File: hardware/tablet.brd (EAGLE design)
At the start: 198 x 124 mm, 0 parts

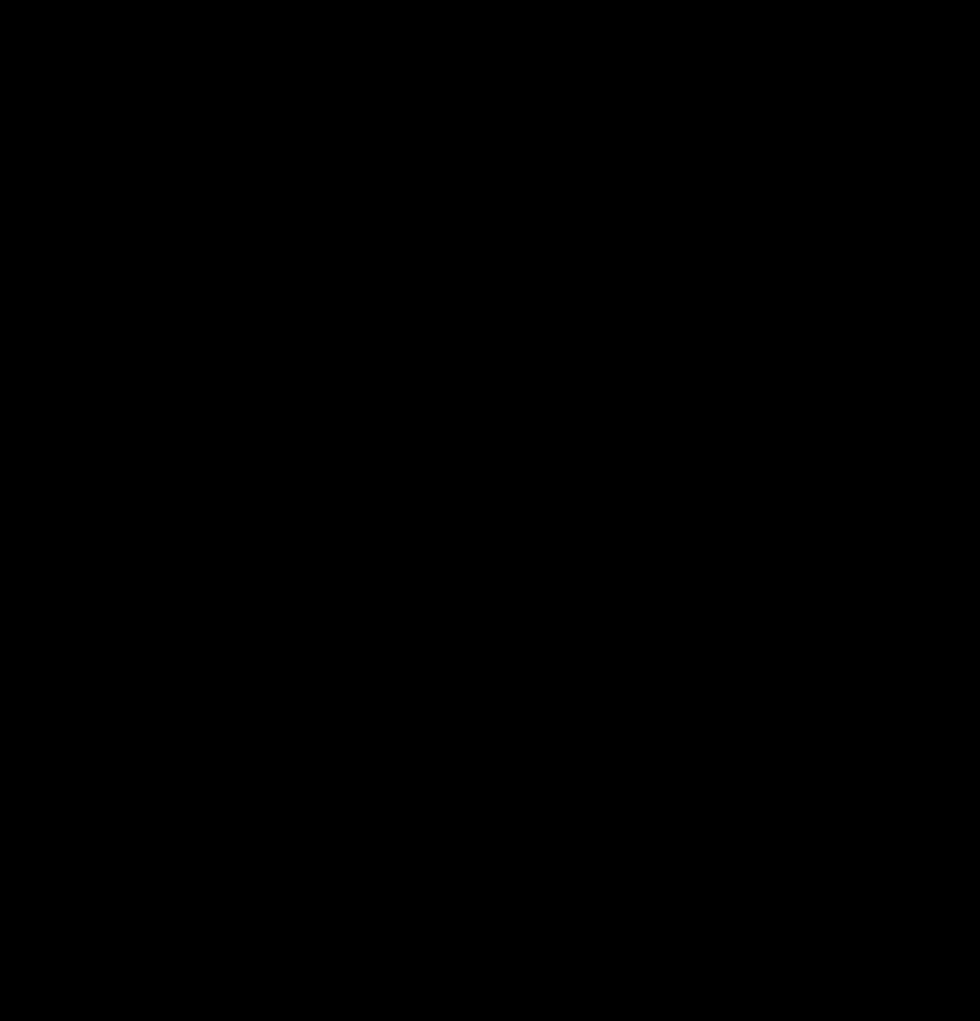
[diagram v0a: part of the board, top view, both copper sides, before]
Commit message: Initial analog front end schematic
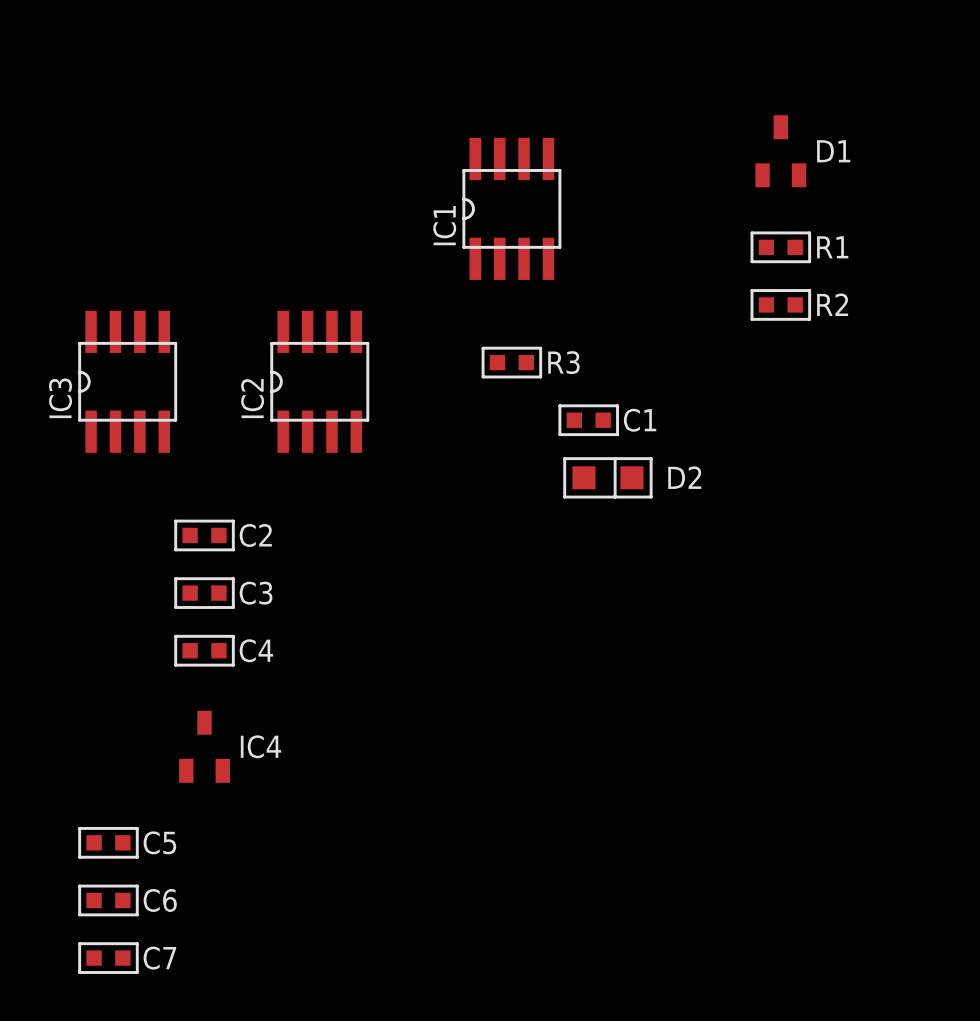
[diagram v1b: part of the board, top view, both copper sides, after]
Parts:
- added C1: ~470pF, 0jpe:0603
- added C2, C3, C4, C5, C6, C7: 100nF, 0jpe:0603
- added D1: BAT721S, 0jpe:SOT23_3
- added D2: 3V9, 0jpe:SOD323
- added IC1: (no value), 0jpe:SOIC8
- added IC2: MCP3201, 0jpe:SOIC8
- added IC3: DG9233EDY, 0jpe:SOIC8
- added IC4: MAX6104EUR, 0jpe:SOT23_3
- added R1: TBD, 0jpe:0603
- added R2, R3: 1K, 0jpe:0603
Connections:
- new net +5V: C2.1, C4.1, C5.1, C7.1, IC1.8, IC2.8, IC3.8, IC4.1
- new net -5V: C3.2, IC1.4
- new net ADC_CS: IC2.5
- new net GND: C2.2, C3.1, C4.2, C5.2, C6.2, C7.2, IC1.2, IC1.5, IC2.3, IC2.4, IC3.4, IC4.3
- new net INT_EN: IC3.7
- new net INT_RST: IC3.3
- new net MISO: IC2.6
- new net N$1: D1.1, IC3.2, R1.2
- new net N$2: D1.2, IC1.3, R1.1, R2.2
- new net N$3: D1.3, IC1.1
- new net N$4: C1.2, D2.1, IC1.6, IC3.6, R3.2
- new net N$6: C6.1, IC2.1, IC4.2
- new net N$7: IC3.1, R3.1
- new net SCLK: IC2.7
- new net SIG: R2.1
- new net VOUT: C1.1, D2.2, IC1.7, IC2.2, IC3.5
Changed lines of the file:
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@@
 </autorouter>
 <elements>
+<element name="D1" library="0jpe" package="SOT23_3" value="BAT721S" x="-99" y="-80"/>
+<element name="R1" library="0jpe" package="0603" value="TBD" x="-99" y="-85"/>
+<element name="R2" library="0jpe" package="0603" value="1K" x="-99" y="-88"/>
+<element name="IC1" library="0jpe" package="SOIC8" value="" x="-113" y="-83"/>
+<element name="R3" library="0jpe" package="0603" value="1K" x="-113" y="-91"/>
+<element name="C1" library="0jpe" package="0603" value="~470pF" x="-109" y="-94"/>
+<element name="D2" library="0jpe" package="SOD323" value="3V9" x="-108" y="-97"/>
+<element name="IC2" library="0jpe" package="SOIC8" value="MCP3201" x="-123" y="-92"/>
+<element name="IC3" library="0jpe" package="SOIC8" value="DG9233EDY" x="-133" y="-92"/>
+<element name="C2" library="0jpe" package="0603" value="100nF" x="-129" y="-100"/>
+<element name="C3" library="0jpe" package="0603" value="100nF" x="-129" y="-103"/>
+<element name="C4" library="0jpe" package="0603" value="100nF" x="-129" y="-106"/>
+<element name="IC4" library="0jpe" package="SOT23_3" value="MAX6104EUR" x="-129" y="-111"/>
+<element name="C5" library="0jpe" package="0603" value="100nF" x="-134" y="-116"/>
+<element name="C6" library="0jpe" package="0603" value="100nF" x="-134" y="-119"/>
+<element name="C7" library="0jpe" package="0603" value="100nF" x="-134" y="-122"/>
 </elements>
 <signals>
+<signal name="N$1">
+<contactref element="D1" pad="1"/>
+<contactref element="R1" pad="2"/>
+<contactref element="IC3" pad="2"/>
+<wire x1="-99.95" y1="-81.25" x2="-133.635" y2="-94.6" width="0" layer="19" extent="1-1"/>
+<wire x1="-98.25" y1="-85" x2="-99.95" y2="-81.25" width="0" layer="19" extent="1-1"/>
+</signal>
+<signal name="N$2">
+<contactref element="D1" pad="2"/>
+<contactref element="R2" pad="2"/>
+<contactref element="R1" pad="1"/>
+<contactref element="IC1" pad="3"/>
+<wire x1="-99.75" y1="-85" x2="-112.365" y2="-85.6" width="0" layer="19" extent="1-1"/>
+<wire x1="-98.25" y1="-88" x2="-99.75" y2="-85" width="0" layer="19" extent="1-1"/>
+<wire x1="-98.05" y1="-81.25" x2="-99.75" y2="-85" width="0" layer="19" extent="1-1"/>
+</signal>
+<signal name="N$3">
+<contactref element="D1" pad="3"/>
+<contactref element="IC1" pad="1"/>
+<wire x1="-99" y1="-78.75" x2="-114.905" y2="-85.6" width="0" layer="19" extent="1-1"/>
+</signal>
+<signal name="SIG">
+<contactref element="R2" pad="1"/>
+</signal>
+<signal name="GND">
+<contactref element="IC1" pad="2"/>
+<contactref element="IC1" pad="5"/>
+<contactref element="IC2" pad="3"/>
+<contactref element="IC2" pad="4"/>
+<contactref element="IC3" pad="4"/>
+<contactref element="C3" pad="1"/>
+<contactref element="C2" pad="2"/>
+<contactref element="C4" pad="2"/>
+<contactref element="IC4" pad="3"/>
+<contactref element="C5" pad="2"/>
+<contactref element="C6" pad="2"/>
+<contactref element="C7" pad="2"/>
+<wire x1="-133.25" y1="-116" x2="-133.25" y2="-119" width="0" layer="19" extent="1-1"/>
+<wire x1="-133.25" y1="-122" x2="-133.25" y2="-119" width="0" layer="19" extent="1-1"/>
+<wire x1="-129" y1="-109.75" x2="-133.25" y2="-116" width="0" layer="19" extent="1-1"/>
+<wire x1="-128.25" y1="-106" x2="-129" y2="-109.75" width="0" layer="19" extent="1-1"/>
+<wire x1="-129.75" y1="-103" x2="-128.25" y2="-106" width="0" layer="19" extent="1-1"/>
+<wire x1="-128.25" y1="-100" x2="-129.75" y2="-103" width="0" layer="19" extent="1-1"/>
+<wire x1="-131.095" y1="-94.6" x2="-128.25" y2="-100" width="0" layer="19" extent="1-1"/>
+<wire x1="-122.365" y1="-94.6" x2="-128.25" y2="-100" width="0" layer="19" extent="1-1"/>
+<wire x1="-121.095" y1="-94.6" x2="-122.365" y2="-94.6" width="0" layer="19" extent="1-1"/>
+<wire x1="-113.635" y1="-85.6" x2="-121.095" y2="-94.6" width="0" layer="19" extent="1-1"/>
+<wire x1="-111.095" y1="-80.4" x2="-113.635" y2="-85.6" width="0" layer="19" extent="1-1"/>
+</signal>
+<signal name="+5V">
+<contactref element="IC1" pad="8"/>
+<contactref element="IC3" pad="8"/>
+<contactref element="C2" pad="1"/>
+<contactref element="C4" pad="1"/>
+<contactref element="IC4" pad="1"/>
+<contactref element="C5" pad="1"/>
+<contactref element="IC2" pad="8"/>
+<contactref element="C7" pad="1"/>
+<wire x1="-134.75" y1="-122" x2="-134.75" y2="-116" width="0" layer="19" extent="1-1"/>
+<wire x1="-129.95" y1="-112.25" x2="-134.75" y2="-116" width="0" layer="19" extent="1-1"/>
+<wire x1="-129.75" y1="-106" x2="-129.95" y2="-112.25" width="0" layer="19" extent="1-1"/>
+<wire x1="-129.75" y1="-100" x2="-129.75" y2="-106" width="0" layer="19" extent="1-1"/>
+<wire x1="-124.905" y1="-89.4" x2="-129.75" y2="-100" width="0" layer="19" extent="1-1"/>
+<wire x1="-134.905" y1="-89.4" x2="-124.905" y2="-89.4" width="0" layer="19" extent="1-1"/>
+<wire x1="-114.905" y1="-80.4" x2="-124.905" y2="-89.4" width="0" layer="19" extent="1-1"/>
+</signal>
+<signal name="-5V">
+<contactref element="IC1" pad="4"/>
+<contactref element="C3" pad="2"/>
+<wire x1="-111.095" y1="-85.6" x2="-128.25" y2="-103" width="0" layer="19" extent="1-1"/>
+</signal>
+<signal name="N$4">
+<contactref element="IC1" pad="6"/>
+<contactref element="R3" pad="2"/>
+<contactref element="C1" pad="2"/>
+<contactref element="D2" pad="1"/>
+<contactref element="IC3" pad="6"/>
+<wire x1="-112.25" y1="-91" x2="-132.365" y2="-89.4" width="0" layer="19" extent="1-1"/>
+<wire x1="-108.25" y1="-94" x2="-112.25" y2="-91" width="0" layer="19" extent="1-1"/>
+<wire x1="-109.25" y1="-97" x2="-108.25" y2="-94" width="0" layer="19" extent="1-1"/>
+<wire x1="-112.365" y1="-80.4" x2="-112.25" y2="-91" width="0" layer="19" extent="1-1"/>
+</signal>
+<signal name="VOUT">
+<contactref element="C1" pad="1"/>
+<contactref element="IC1" pad="7"/>
+<contactref element="D2" pad="2"/>
+<contactref element="IC2" pad="2"/>
+<contactref element="IC3" pad="5"/>
+<wire x1="-123.635" y1="-94.6" x2="-131.095" y2="-89.4" width="0" layer="19" extent="1-1"/>
+<wire x1="-109.75" y1="-94" x2="-123.635" y2="-94.6" width="0" layer="19" extent="1-1"/>
+<wire x1="-106.75" y1="-97" x2="-109.75" y2="-94" width="0" layer="19" extent="1-1"/>
+<wire x1="-113.635" y1="-80.4" x2="-109.75" y2="-94" width="0" layer="19" extent="1-1"/>
+</signal>
+<signal name="N$7">
+<contactref element="IC3" pad="1"/>
+<contactref element="R3" pad="1"/>
+<wire x1="-113.75" y1="-91" x2="-134.905" y2="-94.6" width="0" layer="19" extent="1-1"/>
+</signal>
+<signal name="INT_EN">
+<contactref element="IC3" pad="7"/>
+</signal>
+<signal name="INT_RST">
+<contactref element="IC3" pad="3"/>
+</signal>
+<signal name="N$6">
+<contactref element="C6" pad="1"/>
+<contactref element="IC4" pad="2"/>
+<contactref element="IC2" pad="1"/>
+<wire x1="-128.05" y1="-112.25" x2="-134.75" y2="-119" width="0" layer="19" extent="1-1"/>
+<wire x1="-124.905" y1="-94.6" x2="-128.05" y2="-112.25" width="0" layer="19" extent="1-1"/>
+</signal>
+<signal name="SCLK">
+<contactref element="IC2" pad="7"/>
+</signal>
+<signal name="MISO">
+<contactref element="IC2" pad="6"/>
+</signal>
+<signal name="ADC_CS">
+<contactref element="IC2" pad="5"/>
+</signal>
 </signals>
 </board>

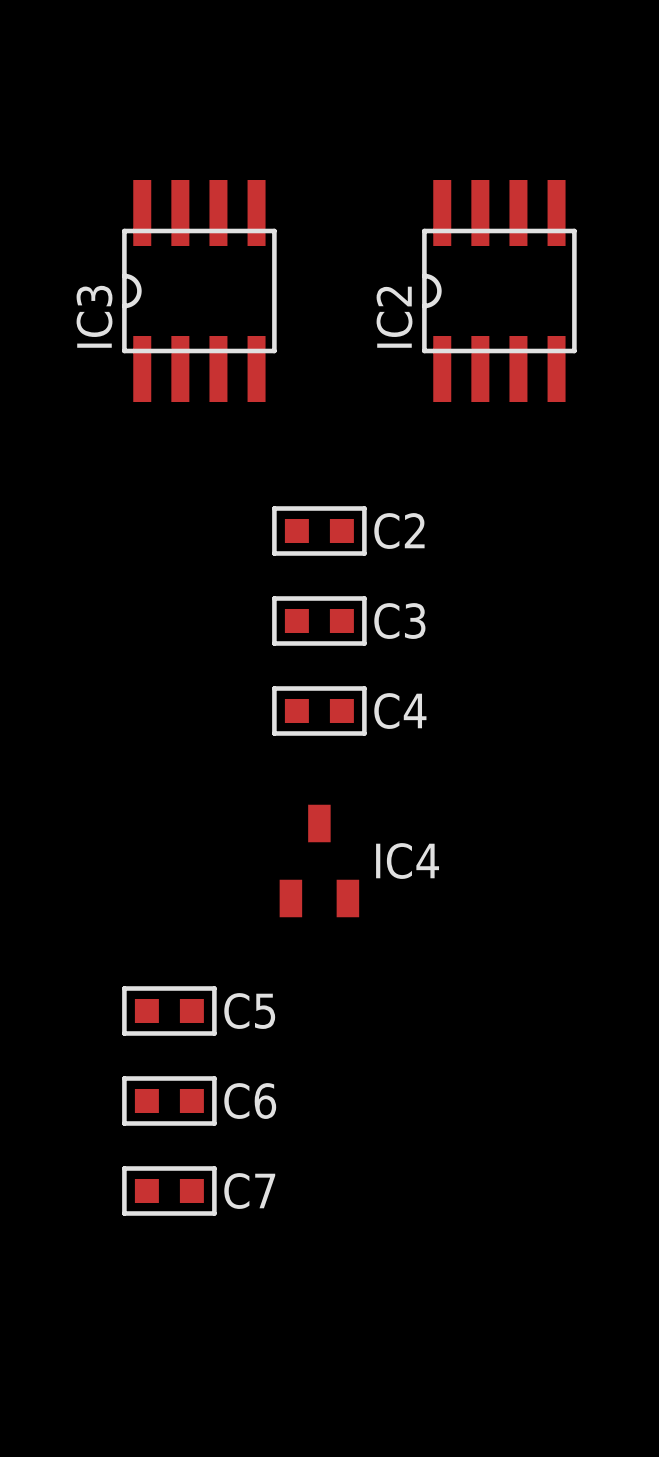
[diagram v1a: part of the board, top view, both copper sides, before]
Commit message: Simplify analog switch layout and increase analog ref load capacitance to ensure stability
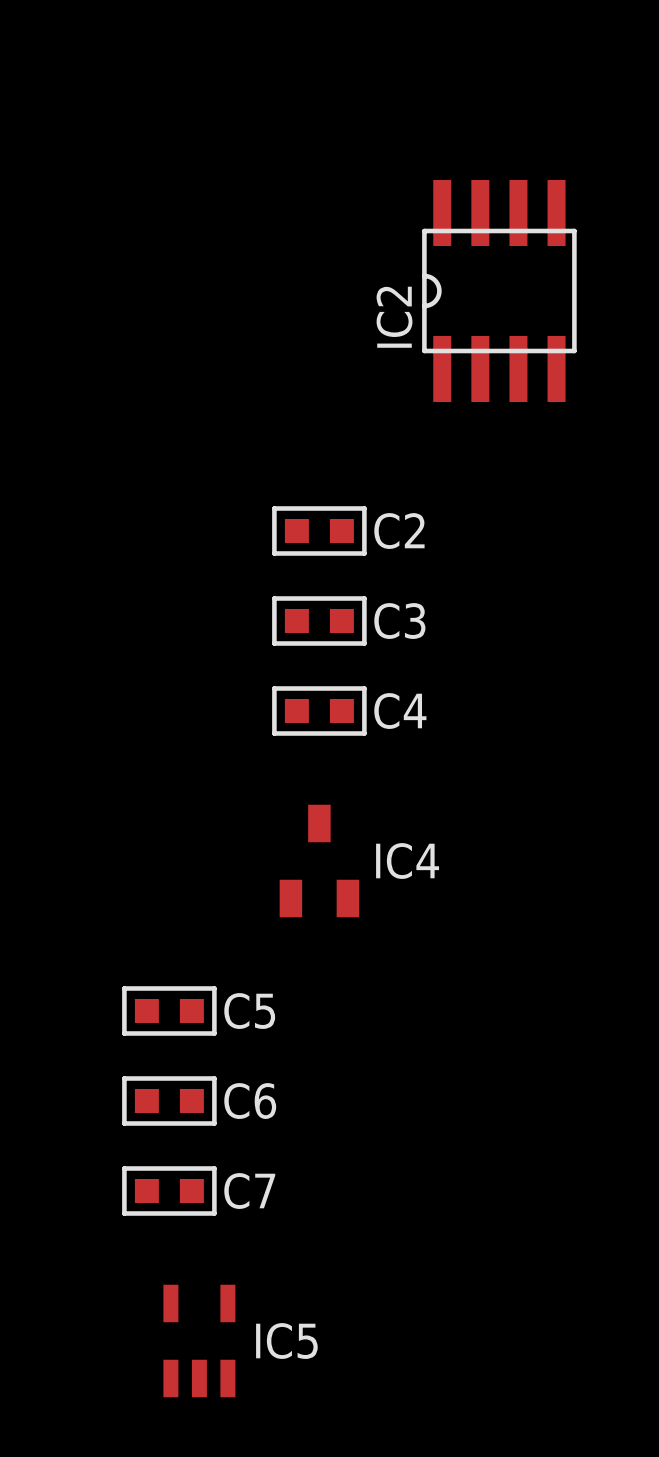
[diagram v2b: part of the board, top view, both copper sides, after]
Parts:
- removed IC3: DG9233EDY, 0jpe:SOIC8
- added IC5: MAX4514EUK, 0jpe:SOT23_5
- C6: value 100nF -> 1uF
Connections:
- removed net INT_EN: IC3.7
- removed net N$7: IC3.1, R3.1
- net +5V: now also IC5.5; no longer IC3.8
- net GND: now also IC5.3; no longer IC3.4
- net INT_RST: now also IC5.4; no longer IC3.3
- net N$1: now also R3.1; no longer IC3.2
- net N$4: now also IC5.1; no longer IC3.6
- net VOUT: now also IC5.2; no longer IC3.5
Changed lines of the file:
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@@
 <element name="D2" library="0jpe" package="SOD323" value="3V9" x="-108" y="-97"/>
 <element name="IC2" library="0jpe" package="SOIC8" value="MCP3201" x="-123" y="-92"/>
-<element name="IC3" library="0jpe" package="SOIC8" value="DG9233EDY" x="-133" y="-92"/>
 <element name="C2" library="0jpe" package="0603" value="100nF" x="-129" y="-100"/>
 <element name="C3" library="0jpe" package="0603" value="100nF" x="-129" y="-103"/>
@@
 <element name="IC4" library="0jpe" package="SOT23_3" value="MAX6104EUR" x="-129" y="-111"/>
 <element name="C5" library="0jpe" package="0603" value="100nF" x="-134" y="-116"/>
-<element name="C6" library="0jpe" package="0603" value="100nF" x="-134" y="-119"/>
+<element name="C6" library="0jpe" package="0603" value="1uF" x="-134" y="-119"/>
 <element name="C7" library="0jpe" package="0603" value="100nF" x="-134" y="-122"/>
+<element name="IC5" library="0jpe" package="SOT23_5" value="MAX4514EUK" x="-133" y="-127"/>
 </elements>
 <signals>
@@
 <contactref element="D1" pad="1"/>
 <contactref element="R1" pad="2"/>
-<contactref element="IC3" pad="2"/>
-<wire x1="-99.95" y1="-81.25" x2="-133.635" y2="-94.6" width="0" layer="19" extent="1-1"/>
-<wire x1="-98.25" y1="-85" x2="-99.95" y2="-81.25" width="0" layer="19" extent="1-1"/>
+<contactref element="R3" pad="1"/>
+<wire x1="-98.25" y1="-85" x2="-113.75" y2="-91" width="0" layer="19" extent="1-1"/>
+<wire x1="-99.95" y1="-81.25" x2="-98.25" y2="-85" width="0" layer="19" extent="1-1"/>
 </signal>
 <signal name="N$2">
@@
 <contactref element="IC2" pad="3"/>
 <contactref element="IC2" pad="4"/>
-<contactref element="IC3" pad="4"/>
 <contactref element="C3" pad="1"/>
 <contactref element="C2" pad="2"/>
@@
 <contactref element="C6" pad="2"/>
 <contactref element="C7" pad="2"/>
+<contactref element="IC5" pad="3"/>
 <wire x1="-133.25" y1="-116" x2="-133.25" y2="-119" width="0" layer="19" extent="1-1"/>
 <wire x1="-133.25" y1="-122" x2="-133.25" y2="-119" width="0" layer="19" extent="1-1"/>
+<wire x1="-132.05" y1="-128.25" x2="-133.25" y2="-122" width="0" layer="19" extent="1-1"/>
 <wire x1="-129" y1="-109.75" x2="-133.25" y2="-116" width="0" layer="19" extent="1-1"/>
 <wire x1="-128.25" y1="-106" x2="-129" y2="-109.75" width="0" layer="19" extent="1-1"/>
 <wire x1="-129.75" y1="-103" x2="-128.25" y2="-106" width="0" layer="19" extent="1-1"/>
 <wire x1="-128.25" y1="-100" x2="-129.75" y2="-103" width="0" layer="19" extent="1-1"/>
-<wire x1="-131.095" y1="-94.6" x2="-128.25" y2="-100" width="0" layer="19" extent="1-1"/>
 <wire x1="-122.365" y1="-94.6" x2="-128.25" y2="-100" width="0" layer="19" extent="1-1"/>
 <wire x1="-121.095" y1="-94.6" x2="-122.365" y2="-94.6" width="0" layer="19" extent="1-1"/>
@@
 <signal name="+5V">
 <contactref element="IC1" pad="8"/>
-<contactref element="IC3" pad="8"/>
 <contactref element="C2" pad="1"/>
 <contactref element="C4" pad="1"/>
@@
 <contactref element="IC2" pad="8"/>
 <contactref element="C7" pad="1"/>
+<contactref element="IC5" pad="5"/>
 <wire x1="-134.75" y1="-122" x2="-134.75" y2="-116" width="0" layer="19" extent="1-1"/>
+<wire x1="-133.95" y1="-125.75" x2="-134.75" y2="-122" width="0" layer="19" extent="1-1"/>
 <wire x1="-129.95" y1="-112.25" x2="-134.75" y2="-116" width="0" layer="19" extent="1-1"/>
 <wire x1="-129.75" y1="-106" x2="-129.95" y2="-112.25" width="0" layer="19" extent="1-1"/>
 <wire x1="-129.75" y1="-100" x2="-129.75" y2="-106" width="0" layer="19" extent="1-1"/>
 <wire x1="-124.905" y1="-89.4" x2="-129.75" y2="-100" width="0" layer="19" extent="1-1"/>
-<wire x1="-134.905" y1="-89.4" x2="-124.905" y2="-89.4" width="0" layer="19" extent="1-1"/>
 <wire x1="-114.905" y1="-80.4" x2="-124.905" y2="-89.4" width="0" layer="19" extent="1-1"/>
 </signal>
@@
 <contactref element="C1" pad="2"/>
 <contactref element="D2" pad="1"/>
-<contactref element="IC3" pad="6"/>
-<wire x1="-112.25" y1="-91" x2="-132.365" y2="-89.4" width="0" layer="19" extent="1-1"/>
-<wire x1="-108.25" y1="-94" x2="-112.25" y2="-91" width="0" layer="19" extent="1-1"/>
-<wire x1="-109.25" y1="-97" x2="-108.25" y2="-94" width="0" layer="19" extent="1-1"/>
+<contactref element="IC5" pad="1"/>
+<wire x1="-108.25" y1="-94" x2="-109.25" y2="-97" width="0" layer="19" extent="1-1"/>
+<wire x1="-112.25" y1="-91" x2="-108.25" y2="-94" width="0" layer="19" extent="1-1"/>
 <wire x1="-112.365" y1="-80.4" x2="-112.25" y2="-91" width="0" layer="19" extent="1-1"/>
+<wire x1="-133.95" y1="-128.25" x2="-109.25" y2="-97" width="0" layer="19" extent="1-1"/>
 </signal>
 <signal name="VOUT">
@@
 <contactref element="D2" pad="2"/>
 <contactref element="IC2" pad="2"/>
-<contactref element="IC3" pad="5"/>
-<wire x1="-123.635" y1="-94.6" x2="-131.095" y2="-89.4" width="0" layer="19" extent="1-1"/>
+<contactref element="IC5" pad="2"/>
 <wire x1="-109.75" y1="-94" x2="-123.635" y2="-94.6" width="0" layer="19" extent="1-1"/>
 <wire x1="-106.75" y1="-97" x2="-109.75" y2="-94" width="0" layer="19" extent="1-1"/>
 <wire x1="-113.635" y1="-80.4" x2="-109.75" y2="-94" width="0" layer="19" extent="1-1"/>
-</signal>
-<signal name="N$7">
-<contactref element="IC3" pad="1"/>
-<contactref element="R3" pad="1"/>
-<wire x1="-113.75" y1="-91" x2="-134.905" y2="-94.6" width="0" layer="19" extent="1-1"/>
-</signal>
-<signal name="INT_EN">
-<contactref element="IC3" pad="7"/>
-</signal>
-<signal name="INT_RST">
-<contactref element="IC3" pad="3"/>
+<wire x1="-133" y1="-128.25" x2="-123.635" y2="-94.6" width="0" layer="19" extent="1-1"/>
 </signal>
 <signal name="N$6">
@@
 <contactref element="IC2" pad="5"/>
 </signal>
+<signal name="INT_RST">
+<contactref element="IC5" pad="4"/>
+</signal>
 </signals>
